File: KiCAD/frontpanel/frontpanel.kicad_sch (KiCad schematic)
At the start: 35 parts, among them J1 8P8C_Shielded, J2 Conn_01x03_Pin, J4 Screw_Terminal_01x04, Q1 2N7000, Q2 2N7000, Q3 2N7000, U1 Adafruit_PCF8575_Breakout, U2 MCP4725, U4 MCP1700x-330xxTO

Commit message: KiCad revB: custom footprints, coax assignments, TO-92 widening, ENC_INT rewire
Second-pass footprint work: filled the remaining empty footprints
that couldn't be handled by the earlier stock-library scripts, added
custom footprints for parts KiCad's stock library doesn't cover, and
did a few schematic hygiene fixes surfaced during the deep-dive
reviews.

Custom footprints (new, xmitter.pretty/):
- SMA_Cinch_142-0701-201_Vertical_JackPCB - 50 Ohm SMA vertical
  through-hole jack for the analog board and bias board coax
  interconnects (I_CATHODE, GRID_CTL, GRID_BLOCK_CRASH, GRID_BIAS).
  Center pin 1.57 mm hole + 4 ground tabs on a 5.08 mm square
  pattern. All 4 ground tabs share pin number 2 (shield).
- CP_Radial_Kemet_ESK_D22.0mm_P10.00mm - Kemet ESK case Q4 radial
  electrolytic (22 mm dia, 10 mm pitch) for C72 = 4700 uF 50V.
- Fuse_Littelfuse_60R_L7.9mm_W3.1mm_P5.08mm - Littelfuse 60R Series
  radial polyfuse for F1 = 60R050XU (0.5 A hold). Body sized for the
  small-body variants (010X-090X); pitch 5.08 mm, drill 0.7 mm.
- C_Axial_Kemet_Aximax_C41X_L4.5mm_D2.6mm_P7.62mm_Horizontal - Kemet
  Aximax C410 axial C0G ceramic for the three 2 pF caps
  (C69/C70/C71) in the vfo_complete keyer chain. Horizontal mount,
  7.62 mm pitch.

New re-runnable script:
- tools/assign_coax_footprints.py - maps
  Connector:Conn_Coaxial_Small symbols to the new Cinch SMA
  footprint. Same "only fill empty, never overwrite" pattern as the
  existing assign_*_footprints.py scripts.

Script extension:
- tools/assign_cap_footprints.py - added value entries for 4700uF
  (Kemet ESK), 220nF (D6 disc), 2pF (Kemet Aximax C41X), and 100uF
  (Vishay 036 RSP). All four entries include the datasheet path and
  the specific case-size rationale.

Schematic edits (all boards):
- 12 coax connectors assigned to the new Cinch SMA footprint
  (analog J17-J19/J23-J24, bias J1/J2/J4/J6/J9/J10/J12) via the new
  assign_coax script.
- 5 caps in vfo_complete assigned via extended assign_cap_footprints
  (C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
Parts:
- Q1, Q2, Q3, U4: footprint Package_TO_SOT_THT:TO-92_Inline -> Package_TO_SOT_THT:TO-92_Inline_Wide
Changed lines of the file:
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@@
 			)
 		)
-		(property "Footprint" "Package_TO_SOT_THT:TO-92_Inline"
+		(property "Footprint" "Package_TO_SOT_THT:TO-92_Inline_Wide"
 			(at 87.63 178.435 0)
 			(hide yes)
@@
 			)
 		)
-		(property "Footprint" "Package_TO_SOT_THT:TO-92_Inline"
+		(property "Footprint" "Package_TO_SOT_THT:TO-92_Inline_Wide"
 			(at 71.12 39.37 0)
 			(hide yes)
@@
 			)
 		)
-		(property "Footprint" "Package_TO_SOT_THT:TO-92_Inline"
+		(property "Footprint" "Package_TO_SOT_THT:TO-92_Inline_Wide"
 			(at 105.41 174.625 0)
 			(hide yes)
@@
 			)
 		)
-		(property "Footprint" "Package_TO_SOT_THT:TO-92_Inline"
+		(property "Footprint" "Package_TO_SOT_THT:TO-92_Inline_Wide"
 			(at 121.92 167.005 0)
 			(hide yes)

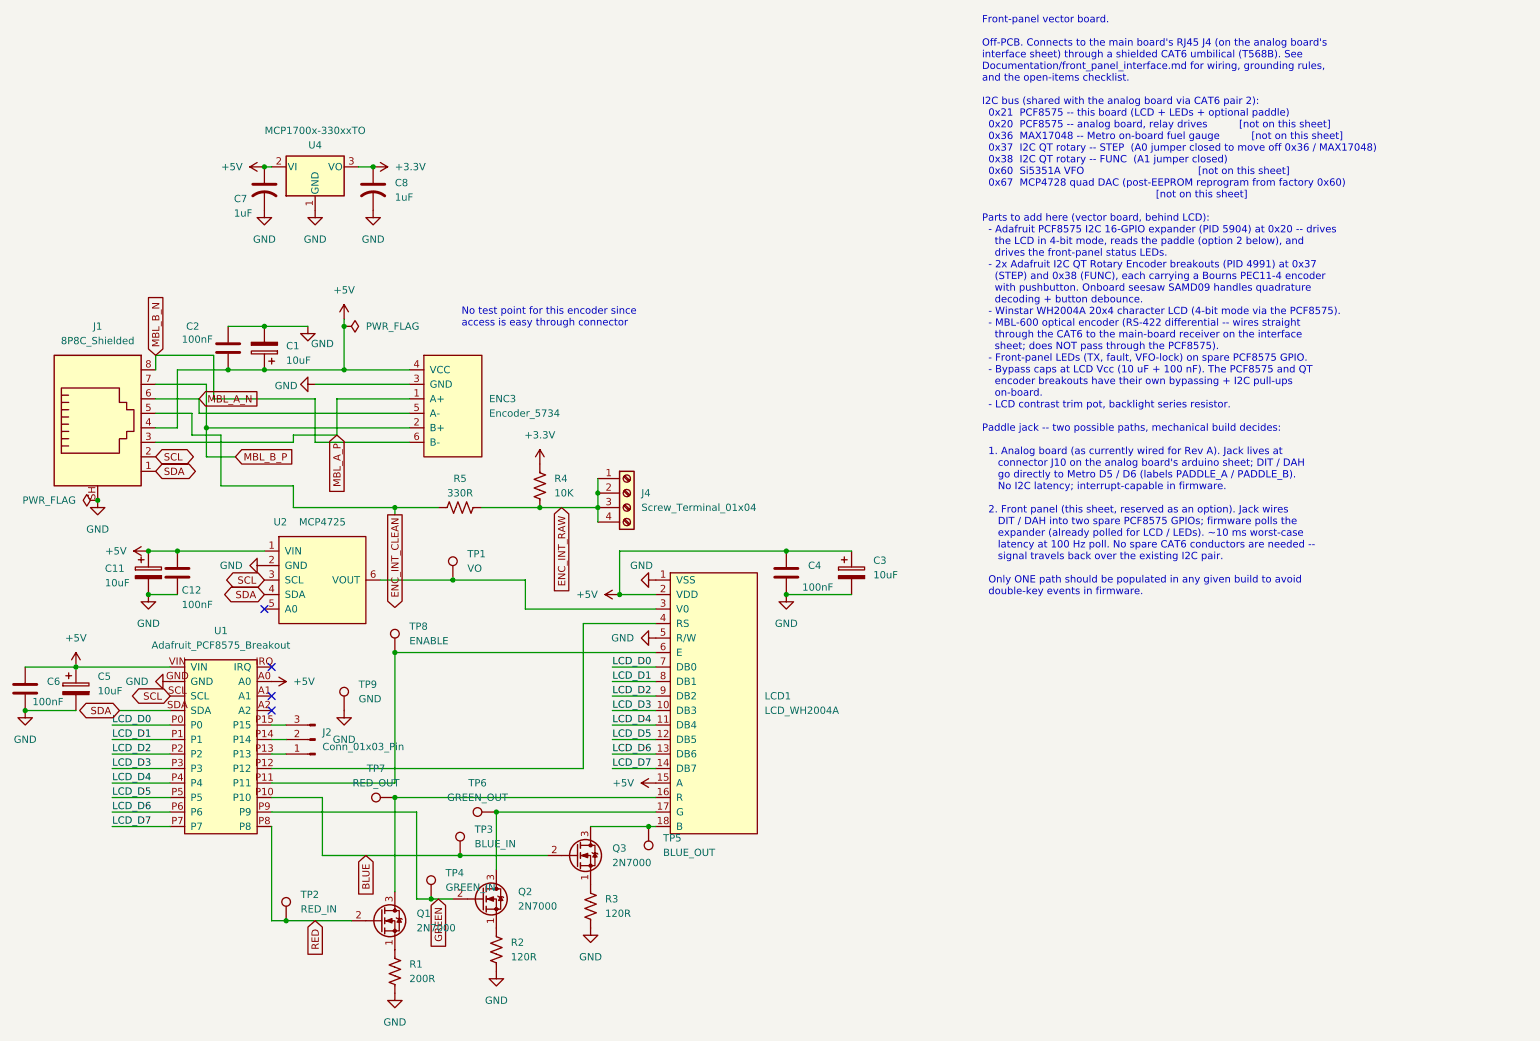
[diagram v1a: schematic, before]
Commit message: revD: ss_pa Option C 5V rail + analog SW1 THT + R/C footprints + doc refresh
ss_pa Option C: swap U13 to LM2936Z-5.0 (full +5V logic rail), re-size
R10 10K->6.8K to preserve ~0.3V fault trip at new rail, drop +3.3V net
entirely. Fixes the previously-dead +5V bus that had no source.

Analog SW1 (Si5351 bringup DPDT): swap SMD footprint for
Button_Switch_THT:SW_CK_JS202011CQN_DPDT_Straight. Verified pin-numbering
convention (pin 1 above pin 6 in THT) matches user's intended DPST
wiring; both SDA/SCL break together.

Analog: assign missing footprints to R3/R4/R5/R8/R9 (DIN0207 axial) and
C4/C5/C6/C7/C8 (disc ceramic 5mm). Add xmitter:DIP-14_W7.62mm.kicad_mod
and 74HCT125 symbol to the xmitter library.

Documentation: Rev D handoff doc updated with M1-M8 fix status, Option C
notes, I2C bus voltage architecture, 74HCT125 SPI shifter, FAULT_N
divider details, and Metro-no-footprint note. Supporting docs updated:
i2c_bus.md full rewrite for 5V HV bus + STEMMA reroute, revD_interconnect
board inventory refresh, status banners on ss_pa.md / Master_Description /
cw_envelope_keyer / front_panel_interface pointing to handoff doc for
items beyond their last-current date.

Co-Authored-By: Claude Opus 4.7 <noreply@anthropic.com>
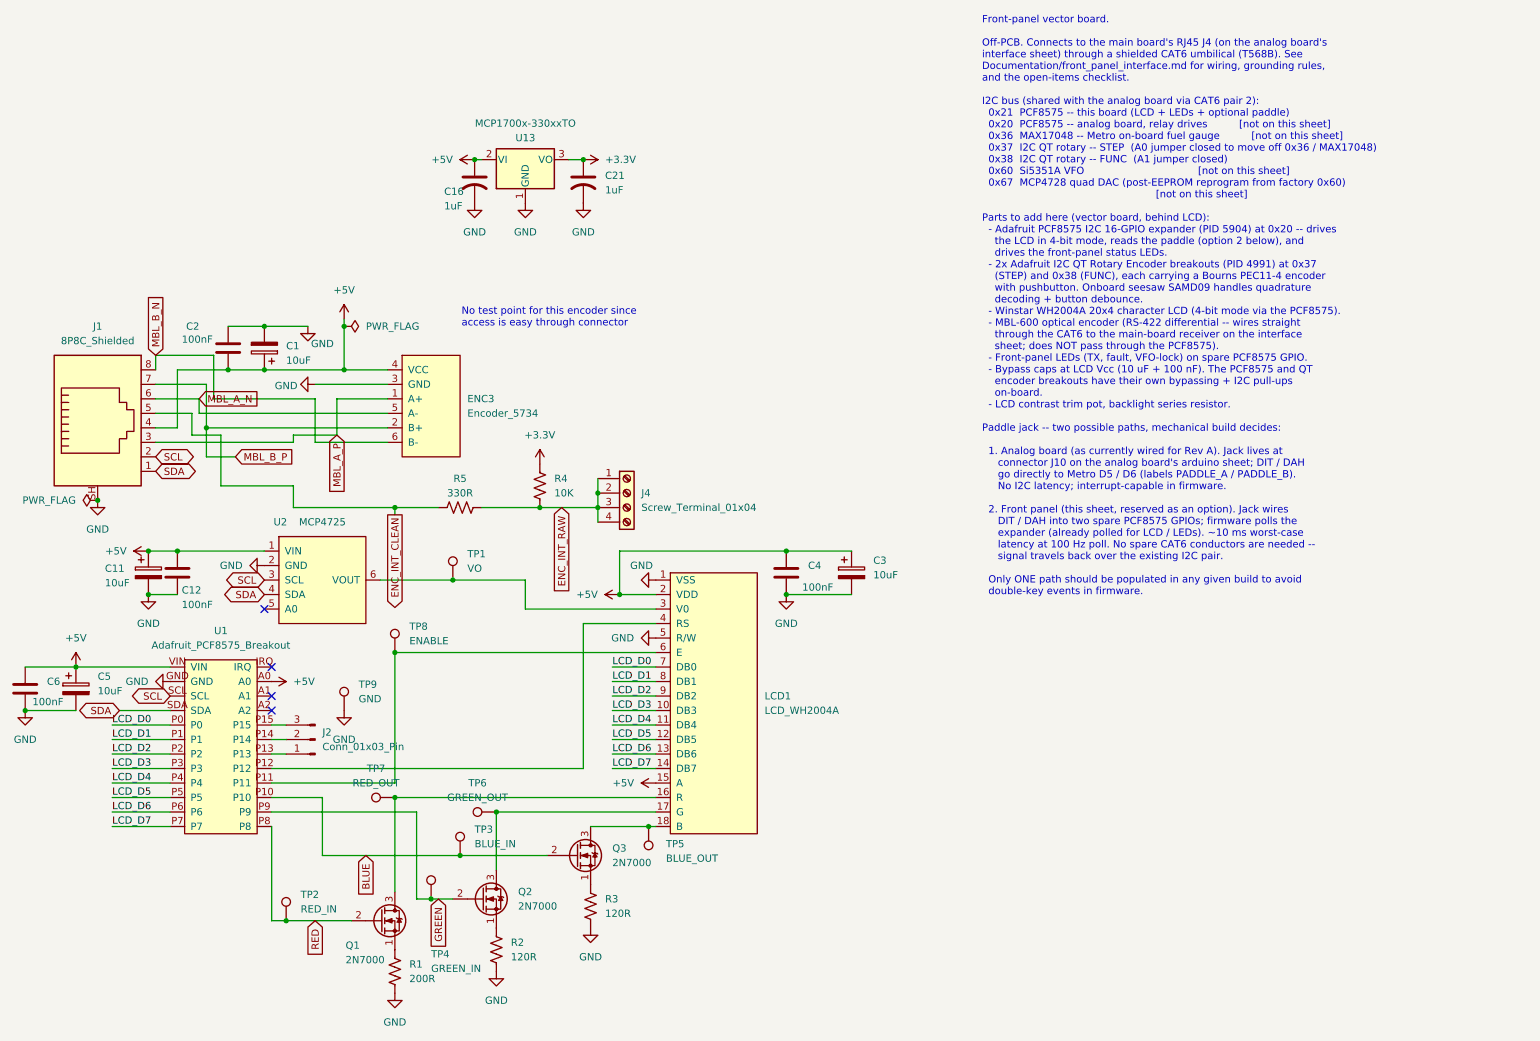
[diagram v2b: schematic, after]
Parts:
- removed C7, C8: 1uF, Capacitor_THT:C_Rect_L7.2mm_W4.5mm_P5.00mm, symbol Device:C_US
- removed U4: MCP1700x-330xxTO, Package_TO_SOT_THT:TO-92_Inline_Wide, symbol Regulator_Linear:MCP1700x-330xxTO
- added C16, C21: 1uF, Capacitor_THT:C_Rect_L7.2mm_W4.5mm_P5.00mm, symbol Device:C_US
- added U13: MCP1700x-330xxTO, Package_TO_SOT_THT:TO-92_Inline_Wide, symbol Regulator_Linear:MCP1700x-330xxTO
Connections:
- net +3.3V: now also C21.1, U13.3 (VO)
- net +5V: now also C16.1, U13.2 (VI)
- net GND: now also C16.2, C21.2, U13.1 (GND)
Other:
- moved on the sheet: ENC3

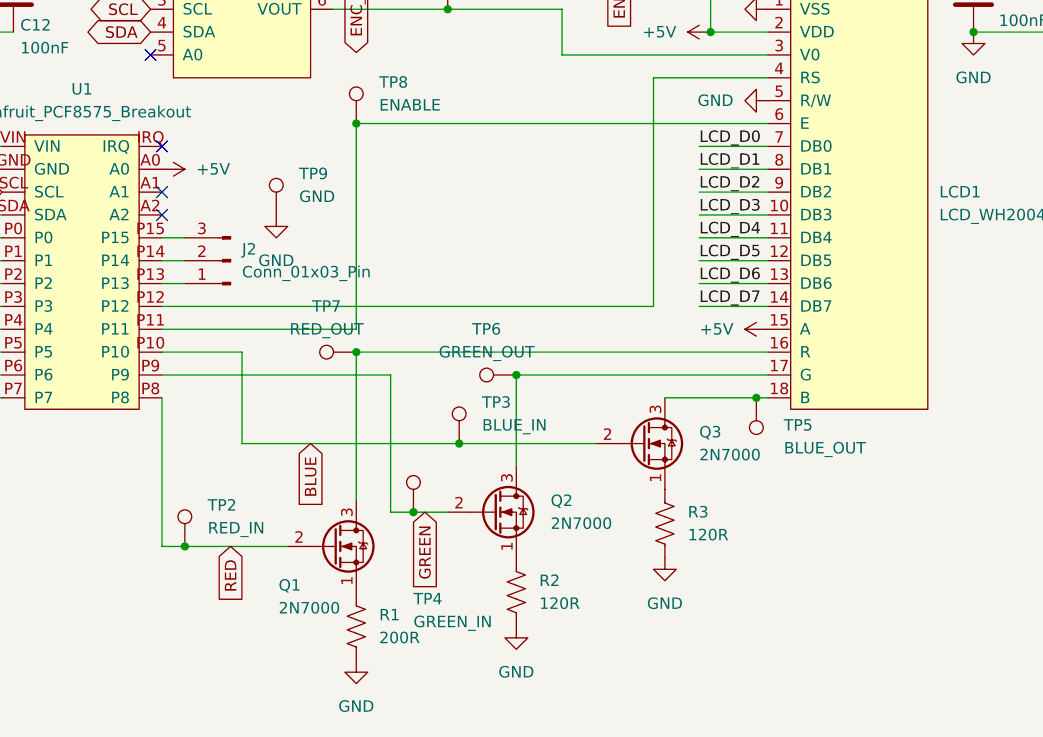
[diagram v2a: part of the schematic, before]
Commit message: revD: frontpanel + Output LPF text updates + protoshield in-progress
Output LPF: K relay Description text fix (pole 2 NC/COM/NO -> NO/COM/NC)
on K1/K2/K3 instances and the embedded lib symbol; CF7/CF8/CF12/CF16
Description "Unpolarized capacitor 2 in parallel to reach" stripped
back to "Unpolarized capacitor"; L6-L20 Descriptions updated T68-6 ->
T50-6 to match footprints.

xmitter.kicad_sym Relay_G6K Description text fix (pole 2 NC/COM/NO ->
NO/COM/NC) so future placements come out right.

Frontpanel: user updates (netlist regenerated).

Protoshield: in-progress schematic touches (new J7, #PWR017). Netlist
intentionally stale -- will regen after Metro-symbol SDA/SCL addition.

Co-Authored-By: Claude Opus 4.7 <noreply@anthropic.com>
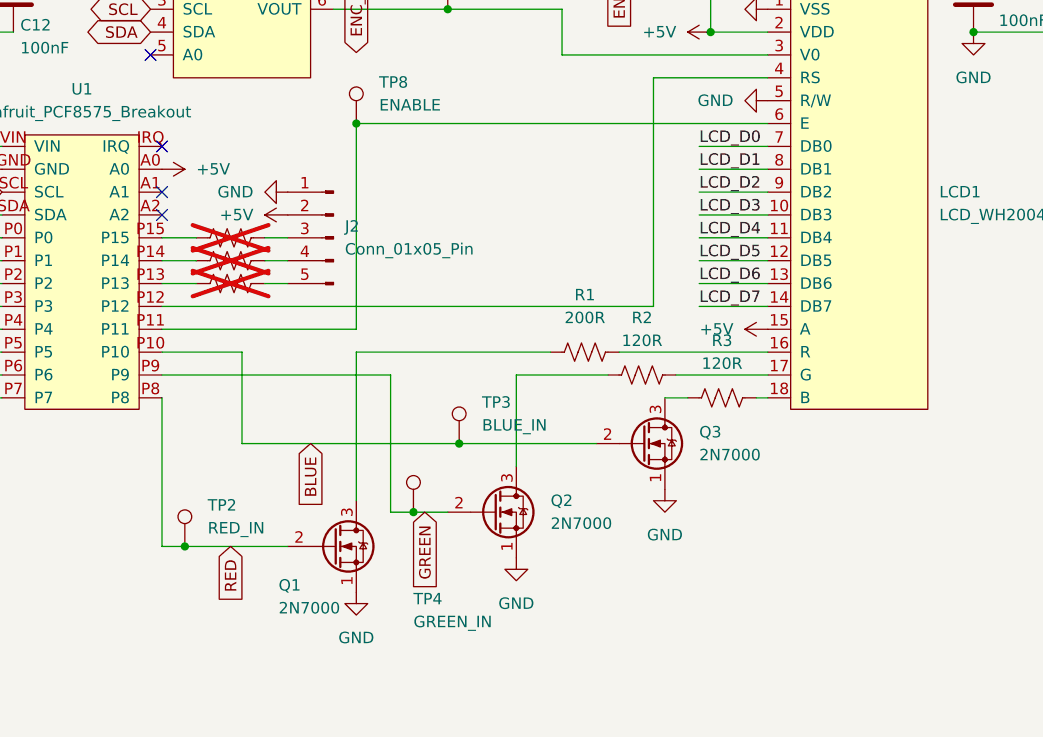
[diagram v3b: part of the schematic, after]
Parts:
- removed J2: Conn_01x03_Pin, Connector_PinHeader_2.54mm:PinHeader_1x03_P2.54mm_Vertical, symbol Connector:Conn_01x03_Pin
- removed TP5: BLUE_OUT, Connector_PinHeader_2.54mm:PinHeader_1x01_P2.54mm_Vertical, symbol xmitter:xTP
- removed TP6: GREEN_OUT, Connector_PinHeader_2.54mm:PinHeader_1x01_P2.54mm_Vertical, symbol xmitter:xTP
- removed TP7: RED_OUT, Connector_PinHeader_2.54mm:PinHeader_1x01_P2.54mm_Vertical, symbol xmitter:xTP
- removed TP9: GND, Connector_PinHeader_2.54mm:PinHeader_1x01_P2.54mm_Vertical, symbol xmitter:xTP
- added J2: Conn_01x05_Pin, symbol Connector:Conn_01x05_Pin
- added R6, R7, R8: 0R, symbol Device:R_US
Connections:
- net +5V: now also J2.2 (Pin_2)
- net GND: now also Q1.1 (S), Q2.1 (S), Q3.1 (S), J2.1 (Pin_1); no longer R1.2, R2.2, R3.2
- net at Q1.3 (D): now also R1.1; no longer LCD1.16 (R)
- net at U1.P13: now also R8.1
- net at U1.P14: now also R7.1
- net at U1.P15: now also R6.1
- net at R2.1: now also Q2.3 (D); no longer Q2.1 (S)
- net at LCD1.17 (G): now also R2.2; no longer Q2.3 (D)
- net at R3.1: now also Q3.3 (D); no longer Q3.1 (S)
- net at LCD1.18 (B): now also R3.2; no longer Q3.3 (D)
- new net: J2.3 (Pin_3), R6.2
- new net: J2.4 (Pin_4), R7.2
- new net: J2.5 (Pin_5), R8.2
- new net: LCD1.16 (R), R1.2

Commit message: revD: footprint pass across all boards + ss_pa fault-chain fix + LLM review brief
- New tools/assign_misc_footprints.py: lib_id-keyed footprint assigner
  (resistors, screw terminals, pin headers, LT1054); mirrors cap-script
  safe-write (UTF-8 no BOM, no CRLF translation).
- tools/assign_cap_footprints.py: added 0.47uF -> C_Rect_L7.0mm case.
- Ran both scripts across analog, ss_pa, Output LPF, frontpanel,
  protoshield, and shelved power board. ~100 fills; details in diffs.
- ss_pa: R1-R4 (0.22 ohm source sense) upgraded to 2W Yageo RSF200
  with DIN0516 L15.5mm/P20.32mm footprint; Value tagged "0.22R 2W".
  R15/R16 confirmed 1/4W (DIN0207) for BS170 source degeneration.
- analog/power: R44 15R 5W horizontal, P30.48mm footprint.
- ss_pa fault chain (from external LLM review): R21/R22 raised
  10K -> 100K to restore self-latching loop gain; new R26 = 100K
  across C12 so cap discharges between power cycles (reliable reset).
  R26 footprint pending.
- Documentation/revD_llm_review_brief.md: new, comprehensive system
  description for external LLM deep-dive (function, component values,
  power dissipation, design flaws). References all five board netlists.

Co-Authored-By: Claude Opus 4.7 <noreply@anthropic.com>
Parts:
- J2: footprint (none) -> Connector_PinHeader_2.54mm:PinHeader_1x05_P2.54mm_Vertical
- R6, R7, R8: footprint (none) -> Resistor_THT:R_Axial_DIN0207_L6.3mm_D2.5mm_P10.16mm_Horizontal
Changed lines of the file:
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@@
 			)
 		)
-		(property "Footprint" ""
+		(property "Footprint" "Resistor_THT:R_Axial_DIN0207_L6.3mm_D2.5mm_P10.16mm_Horizontal"
 			(at 71.374 141.224 90)
 			(hide yes)
@@
 			)
 		)
-		(property "Footprint" ""
+		(property "Footprint" "Connector_PinHeader_2.54mm:PinHeader_1x05_P2.54mm_Vertical"
 			(at 82.55 142.24 0)
 			(hide yes)
@@
 			)
 		)
-		(property "Footprint" ""
+		(property "Footprint" "Resistor_THT:R_Axial_DIN0207_L6.3mm_D2.5mm_P10.16mm_Horizontal"
 			(at 71.374 143.764 90)
 			(hide yes)
@@
 			)
 		)
-		(property "Footprint" ""
+		(property "Footprint" "Resistor_THT:R_Axial_DIN0207_L6.3mm_D2.5mm_P10.16mm_Horizontal"
 			(at 71.374 146.304 90)
 			(hide yes)
